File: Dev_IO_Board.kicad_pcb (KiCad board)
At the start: 4 copper layers, 127 x 87.6 mm, 72 parts, among them J1 Conn_01x20_Pin, J2 Conn_01x20_Pin, Q1 KRC110S, U1 H3LIS331DLTR, U2 74LS49, U3 74LS49, U4 D148K, U5 D148K

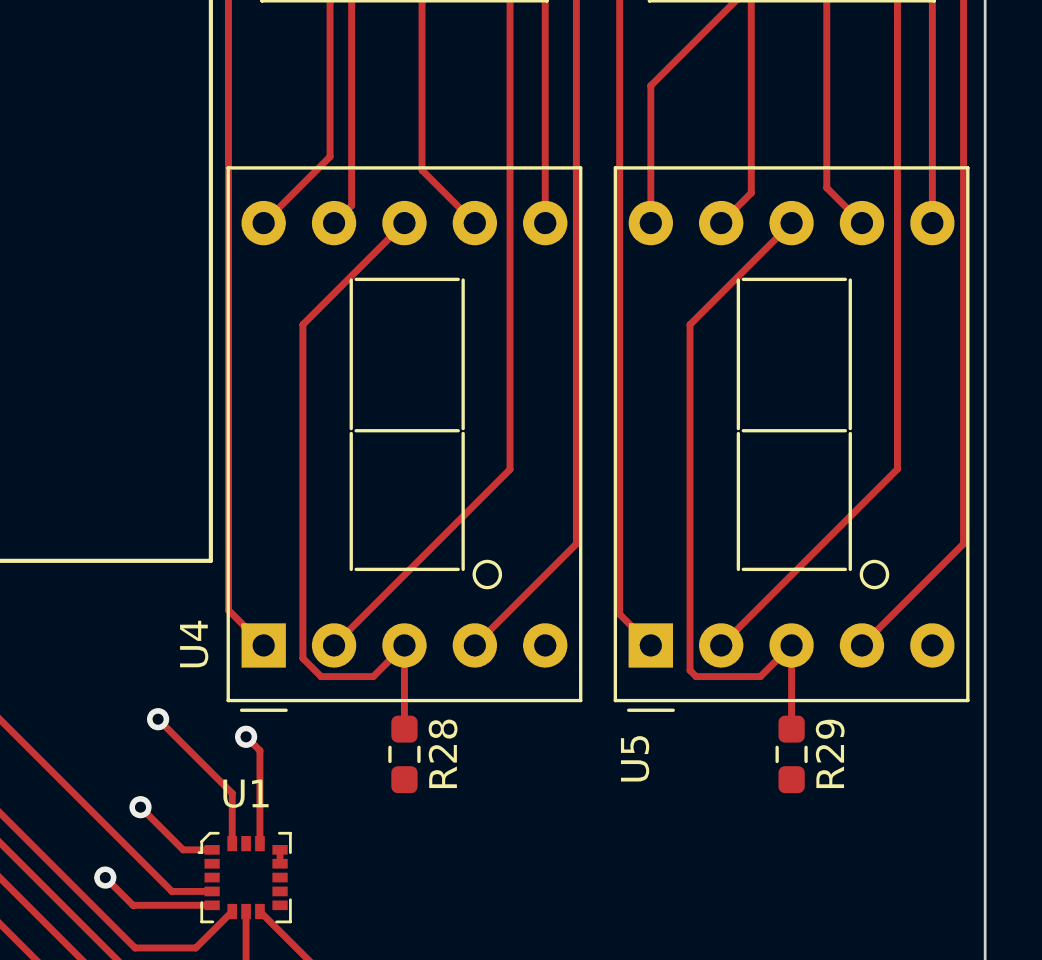
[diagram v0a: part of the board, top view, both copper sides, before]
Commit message: Changed segment display to TDSR1360
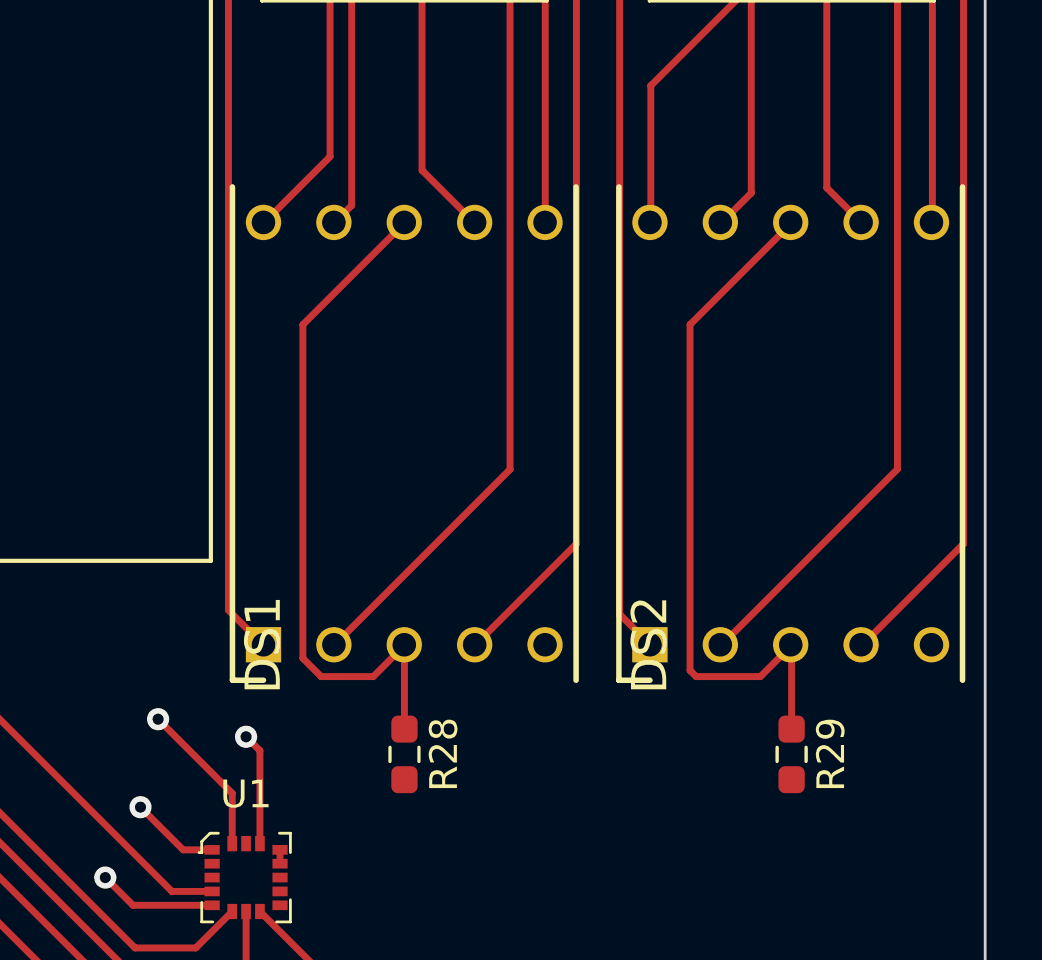
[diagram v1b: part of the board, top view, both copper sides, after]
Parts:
- removed U4, U5: D148K, Display_7Segment:D1X8K
- added DS1: TDSR1360, SamacSys_Parts:DIPS1524W55P254L1225H710Q10N, F.Cu at (184.7, 101.3)
- added DS2: TDSR1360, SamacSys_Parts:DIPS1524W55P254L1225H710Q10N, F.Cu at (198.6, 101.3)
